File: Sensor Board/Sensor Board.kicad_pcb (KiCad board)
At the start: 4 copper layers, 41.7 x 49.5 mm, 61 parts, among them J1 Programming Header, J2 CAN Bus Connector, J3 Micro_SD_Card, U1 PIC18F26K83, U2 INA180, U3 MCP2562, U4 OPA323, U5 MCP3561-E/ST, U6 SPX3819M5-L-3-3, U7 MCP1501-25xSN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

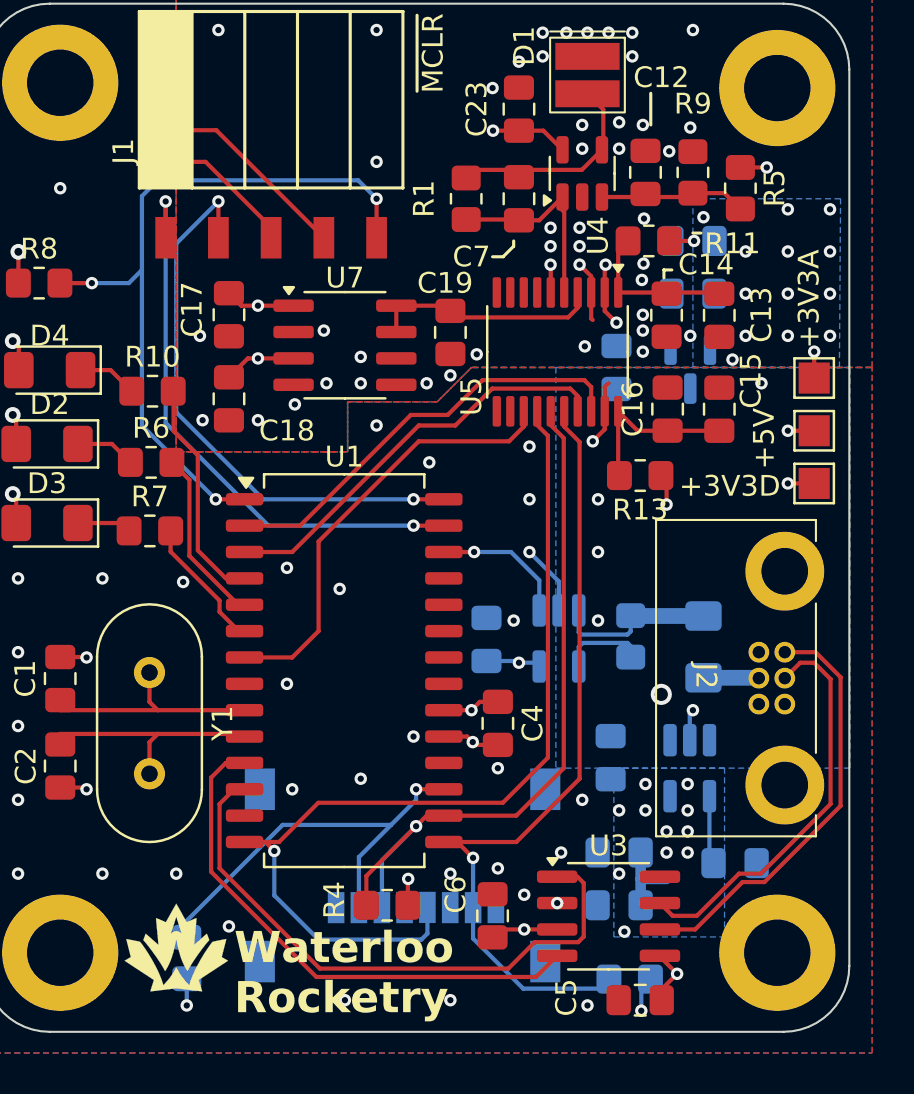
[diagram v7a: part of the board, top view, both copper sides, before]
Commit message: implemented Joe's comments
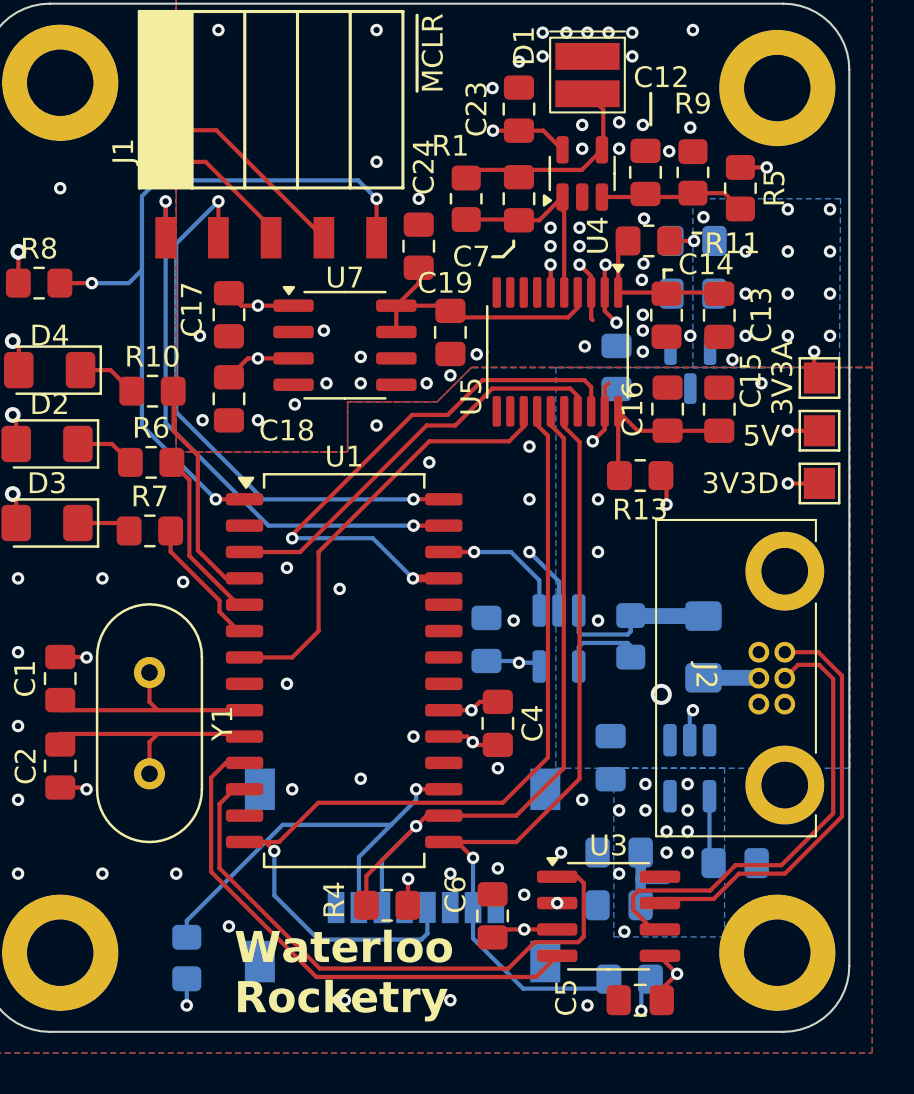
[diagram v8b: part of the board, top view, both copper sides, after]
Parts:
- removed +3V3A: 3V3A, TestPoint:TestPoint_Pad_1.5x1.5mm
- removed +3V3D: 3V3D, TestPoint:TestPoint_Pad_1.5x1.5mm
- removed +5V: 5v, TestPoint:TestPoint_Pad_1.5x1.5mm
- removed G***: LOGO, Team_Logo:Logo_SilkScreen_5mm
- added 3V3A: 3V3A, TestPoint:TestPoint_Pad_1.5x1.5mm, F.Cu at (222.0, 72.6)
- added 3V3D: 3V3D, TestPoint:TestPoint_Pad_1.5x1.5mm, F.Cu at (222.0, 77.7)
- added 5V: 5v, TestPoint:TestPoint_Pad_1.5x1.5mm, F.Cu at (222.0, 75.2)
- added C24: 10uF, Capacitor_SMD:C_0805_2012Metric_Pad1.18x1.45mm_HandSolder, F.Cu at (202.7, 66.3)
- C6: value 0.1uF -> 10uF
- R10: value 220R -> 90R
- R12: value 200mR -> 93.1mR
- R6, R7: value 120R -> 150R
- U7: value MCP1501-25xSN -> MCP1501-30xSN
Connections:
- H1 pad 1: unconnected-(H1-Pad1) -> AGND
- J2 pad 2: /CANH -> /CANL
- J2 pad 3: /CANL -> /CANH
- U1 pad 2: /MCLKIN -> unconnected-(U1-RA0-Pad2)
- U1 pad 25: unconnected-(U1-RB4-Pad25) -> /MCLKIN
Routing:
- net /MCLKIN: track 20.9 -> 27.1 mm, vias 0 -> 2
- net /CANL: track 20.6 -> 23.0 mm
- net Net-(U5-REFIN+): track 11.2 -> 13.4 mm
- net /CANH: track 19.6 -> 20.5 mm
- net AGND: vias 47 -> 48
